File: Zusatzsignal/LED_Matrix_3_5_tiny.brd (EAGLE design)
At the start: 15.8 x 21.6 mm, 18 parts, among them IC3 ATTINY44SSU, Q1 IRLML5203, Q2 IRLML5203, Q3 IRLML5203, Q4 IRLML5203, Q5 IRLML5203, X1 TSW-106-02-S-S, X2 TSW-106-02-S-S-RA

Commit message: Verbesserung der Zusatzanzeigerplatine
- Änderung des Layouts der Rückseite
- Änderung der Durchführungen auf RM
- Beseitigung von DRC-Fehlern
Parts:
- removed S1, S2, S3, S4, S5: (no value), pinhead:1X01
- added X3: SSW-102-02-S-S, con-samtec:SSW-102-02-S-S
- added X4: SSW-103-02-S-S, con-samtec:SSW-103-02-S-S
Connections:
- net N$19: now also X3.2; no longer S5.1
- net N$20: now also X3.1; no longer S4.1
- net N$21: now also X4.3; no longer S3.1
- net N$22: now also X4.2; no longer S2.1
- net N$23: now also X4.1; no longer S1.1

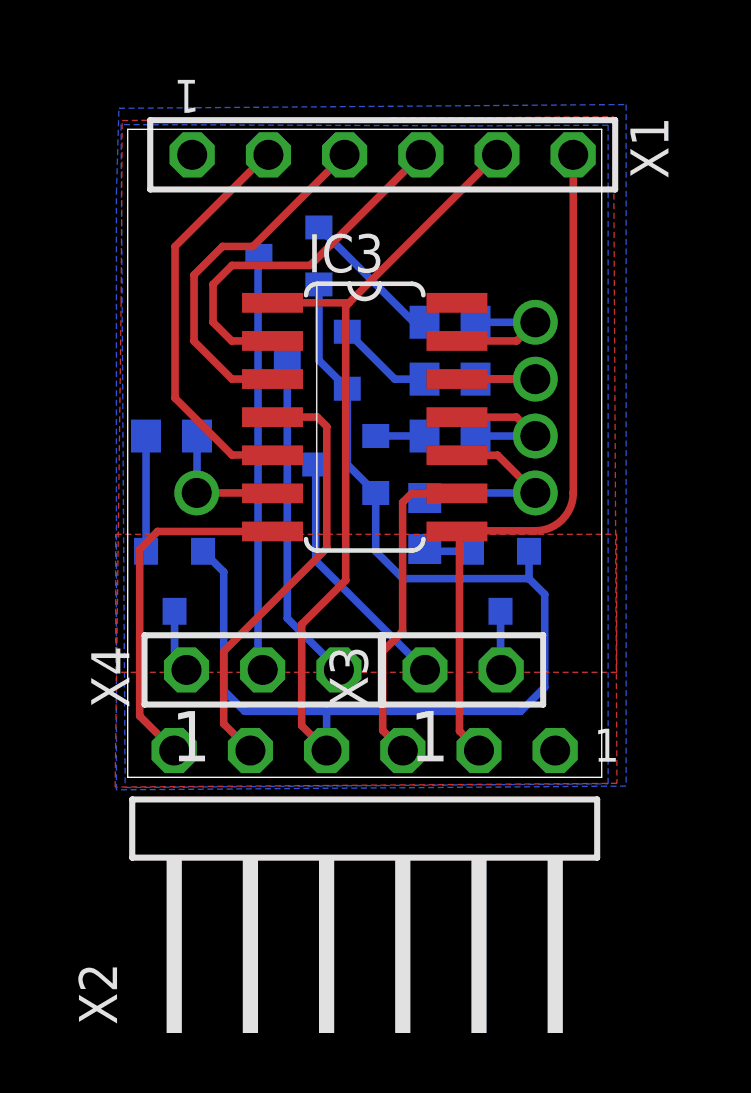
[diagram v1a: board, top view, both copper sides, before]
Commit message: Neuorganisation des Zusatzanzeigers
-> Werte begradigt und alle LEDs korrigiert
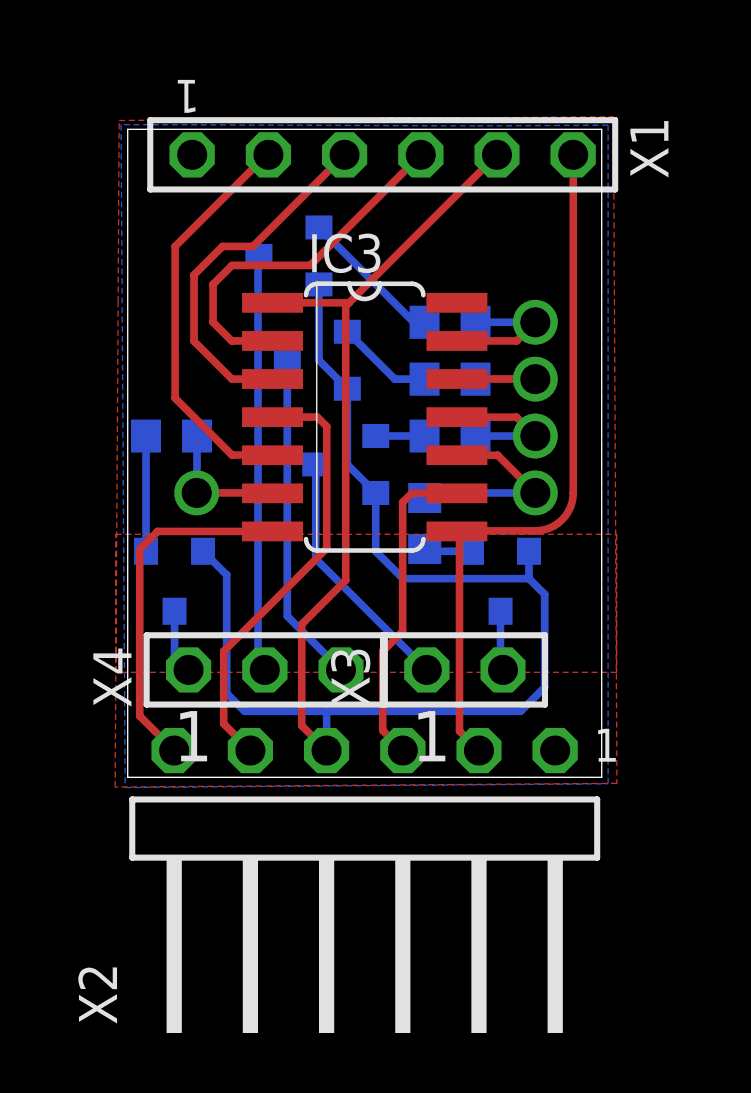
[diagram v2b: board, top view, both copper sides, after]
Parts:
- moved X4 0.07 mm to (4.57, 3.58)
- moved X3 0.06 mm to (11.2, 3.58)
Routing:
- removed copper zone on layer 16, net N$14
